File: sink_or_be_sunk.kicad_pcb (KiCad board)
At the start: 2 copper layers, 87 parts, among them J1 Keypad_Conn, J10 Grid_Conn, J11 Grid_Conn, J12 Grid_Conn, J13 Grid_Conn, J14 Grid_Conn, J15 Grid_Conn, J16 Grid_Conn, J17 Grid_Conn, J18 Grid_Conn, J19 Grid_Conn, J2 Mux_Conn, J20 Grid_Conn, J21 Grid_Conn, J22 Grid_Conn, J23 Grid_Conn, J3 Display_Conn, J4 JTAG_Conn, J5 Battery_Conn, J6 USB_B_Micro, J7 Debug_Conn, J8 Grid_Conn_LED, J9 Grid_Conn, M1 Motor_DC, Q1 IRL530, Q2 2N3704, Q3 2N3704, Q4 Q_PMOS_DGS, SW1 Reset_SW, SW2 SW_DPST, U1 SN74HC151N, U2 LDL1117-SMD, U3 MCP73831-2-OT, U4 MCP608, U5 ESP32-WROOM-32, U6 CY7C65213A-28PVXI

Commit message: before pin shift
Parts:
- moved J7 41.9 mm to (396.3, 130.0)
- moved TP2 14.8 mm to (476.7, 94.6)
- moved J4 14.6 mm to (490.9, 95.8)
- moved R24 14.0 mm to (485.4, 90.7)
- moved TP1 14.0 mm to (476.8, 100.2)
- moved R25 13.9 mm to (485.4, 93.3)
- moved R26 13.5 mm to (485.3, 95.8)
- moved R22 13.2 mm to (485.3, 88.2)
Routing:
- net /RXLED: track 0.00 -> 36.5 mm, vias 0 -> 1
- net /TXLED: track 0.00 -> 35.5 mm, vias 0 -> 1
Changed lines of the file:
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@@
     (thickness 1.6)
     (drawings 2)
-    (tracks 180)
+    (tracks 194)
     (zones 0)
     (modules 87)
@@
   )
   (module TestPoint:TestPoint_Plated_Hole_D2.0mm (layer F.Cu)
-    (at 464.058 86.868)
+    (at 476.7072 94.5896)
     (descr "Plated Hole as test Point, diameter 2.0mm")
     (tags "test point plated hole")
@@
   )
   (module TestPoint:TestPoint_Plated_Hole_D2.0mm (layer F.Cu)
-    (at 472.186 86.995)
+    (at 476.758 100.2284)
     (descr "Plated Hole as test Point, diameter 2.0mm")
     (tags "test point plated hole")
@@
   )
   (module Resistor_SMD:R_0805_2012Metric_Pad1.20x1.40mm_HandSolder (layer F.Cu)
-    (at 494.411 85.852)
+    (at 485.3084 95.8088)
     (descr "Resistor SMD 0805 (2012 Metric), square (rectangular) end terminal, IPC_7351 nominal with elongated pad for handsoldering. (Body size source: IPC-SM-782 page 72, https://www.pcb-3d.com/wordpress/wp-content/uploads/ipc-sm-782a_amendment_1_and_2.pdf), generated with kicad-footprint-generator")
     (tags "resistor handsolder")
@@
   )
   (module Resistor_SMD:R_0805_2012Metric_Pad1.20x1.40mm_HandSolder (layer F.Cu)
-    (at 494.157 82.423)
+    (at 485.394 93.2688)
     (descr "Resistor SMD 0805 (2012 Metric), square (rectangular) end terminal, IPC_7351 nominal with elongated pad for handsoldering. (Body size source: IPC-SM-782 page 72, https://www.pcb-3d.com/wordpress/wp-content/uploads/ipc-sm-782a_amendment_1_and_2.pdf), generated with kicad-footprint-generator")
     (tags "resistor handsolder")
@@
   )
   (module Resistor_SMD:R_0805_2012Metric_Pad1.20x1.40mm_HandSolder (layer F.Cu)
-    (at 494.157 79.756)
+    (at 485.394 90.7288)
     (descr "Resistor SMD 0805 (2012 Metric), square (rectangular) end terminal, IPC_7351 nominal with elongated pad for handsoldering. (Body size source: IPC-SM-782 page 72, https://www.pcb-3d.com/wordpress/wp-content/uploads/ipc-sm-782a_amendment_1_and_2.pdf), generated with kicad-footprint-generator")
     (tags "resistor handsolder")
@@
   )
   (module Resistor_SMD:R_0805_2012Metric_Pad1.20x1.40mm_HandSolder (layer F.Cu)
-    (at 493.141 77.597)
+    (at 485.3432 88.1888)
     (descr "Resistor SMD 0805 (2012 Metric), square (rectangular) end terminal, IPC_7351 nominal with elongated pad for handsoldering. (Body size source: IPC-SM-782 page 72, https://www.pcb-3d.com/wordpress/wp-content/uploads/ipc-sm-782a_amendment_1_and_2.pdf), generated with kicad-footprint-generator")
     (tags "resistor handsolder")
@@
   )
   (module Connector_PinHeader_2.54mm:PinHeader_1x02_P2.54mm_Vertical (layer F.Cu)
-    (at 436.245 142.621 270)
+    (at 396.2908 130.048 270)
     (descr "Through hole straight pin header, 1x02, 2.54mm pitch, single row")
     (tags "Through hole pin header THT 1x02 2.54mm single row")
@@
   )
   (module Connector_PinHeader_2.54mm:PinHeader_1x04_P2.54mm_Vertical (layer F.Cu)
-    (at 501.142 85.344 180)
+    (at 490.9312 95.8088 180)
     (descr "Through hole straight pin header, 1x04, 2.54mm pitch, single row")
     (tags "Through hole pin header THT 1x04 2.54mm single row")
@@
   (segment (start 448.183 97.0885) (end 448.269 97.1745) (width 0.254) (layer F.Cu) (net 2))
   (segment (start 448.183 95.005) (end 448.183 97.0885) (width 0.254) (layer F.Cu) (net 2))
-  (via (at 448.31 99.06) (size 0.762) (drill 0.381) (layers F.Cu B.Cu) (net 2))
-  (segment (start 448.269 99.019) (end 448.31 99.06) (width 0.254) (layer F.Cu) (net 2))
-  (segment (start 448.269 97.1745) (end 448.269 99.019) (width 0.254) (layer F.Cu) (net 2))
   (segment (start 449.453 111.134) (end 449.453 113.03) (width 0.8128) (layer F.Cu) (net 2))
   (segment (start 445.0625 106.7435) (end 449.453 111.134) (width 0.8128) (layer F.Cu) (net 2))
   (segment (start 445.019 103.346663) (end 444.551847 102.87951) (width 0.254) (layer F.Cu) (net 2))
-  (segment (start 448.31 99.06) (end 444.551847 102.818153) (width 0.254) (layer B.Cu) (net 2))
   (segment (start 445.019 104.3745) (end 445.019 103.346663) (width 0.254) (layer F.Cu) (net 2))
   (via (at 444.551847 102.87951) (size 0.762) (drill 0.381) (layers F.Cu B.Cu) (net 2))
+  (segment (start 448.269 97.1745) (end 448.269 99.019) (width 0.254) (layer F.Cu) (net 2))
   (segment (start 444.551847 102.818153) (end 444.551847 102.87951) (width 0.254) (layer B.Cu) (net 2))
+  (via (at 448.31 99.06) (size 0.762) (drill 0.381) (layers F.Cu B.Cu) (net 2))
+  (segment (start 448.31 99.06) (end 444.551847 102.818153) (width 0.254) (layer B.Cu) (net 2))
+  (segment (start 448.269 99.019) (end 448.31 99.06) (width 0.254) (layer F.Cu) (net 2))
   (segment (start 424.951 130.683) (end 425.069 130.565) (width 0.8128) (layer F.Cu) (net 3))
   (segment (start 421.8215 130.683) (end 424.951 130.683) (width 0.8128) (layer F.Cu) (net 3))
@@
   (segment (start 438.107 127.465) (end 440.055 129.413) (width 0.254) (layer F.Cu) (net 5))
   (segment (start 435.991 127.465) (end 438.107 127.465) (width 0.254) (layer F.Cu) (net 5))
+  (via (at 445.2112 99.9236) (size 0.762) (drill 0.381) (layers F.Cu B.Cu) (net 6))
+  (segment (start 445.3489 99.9236) (end 445.2112 99.9236) (width 0.254) (layer F.Cu) (net 6))
+  (segment (start 446.969 98.3035) (end 445.3489 99.9236) (width 0.254) (layer F.Cu) (net 6))
+  (segment (start 446.969 97.1745) (end 446.969 98.3035) (width 0.254) (layer F.Cu) (net 6))
+  (segment (start 474.881599 98.351999) (end 476.758 100.2284) (width 0.254) (layer B.Cu) (net 6))
+  (segment (start 447.970159 98.351999) (end 474.881599 98.351999) (width 0.254) (layer B.Cu) (net 6))
+  (segment (start 446.398558 99.9236) (end 447.970159 98.351999) (width 0.254) (layer B.Cu) (net 6))
+  (segment (start 445.2112 99.9236) (end 446.398558 99.9236) (width 0.254) (layer B.Cu) (net 6))
+  (via (at 445.3636 98.9076) (size 0.762) (drill 0.381) (layers F.Cu B.Cu) (net 7))
+  (segment (start 445.7149 98.9076) (end 445.3636 98.9076) (width 0.254) (layer F.Cu) (net 7))
+  (segment (start 446.319 98.3035) (end 445.7149 98.9076) (width 0.254) (layer F.Cu) (net 7))
+  (segment (start 446.319 97.1745) (end 446.319 98.3035) (width 0.254) (layer F.Cu) (net 7))
+  (segment (start 449.6816 94.5896) (end 476.7072 94.5896) (width 0.254) (layer B.Cu) (net 7))
+  (segment (start 445.3636 98.9076) (end 449.6816 94.5896) (width 0.254) (layer B.Cu) (net 7))
   (via (at 406.8445 116.205) (size 0.762) (drill 0.381) (layers F.Cu B.Cu) (net 24))
   (segment (start 406.0825 115.443) (end 406.8445 116.205) (width 0.254) (layer F.Cu) (net 24))

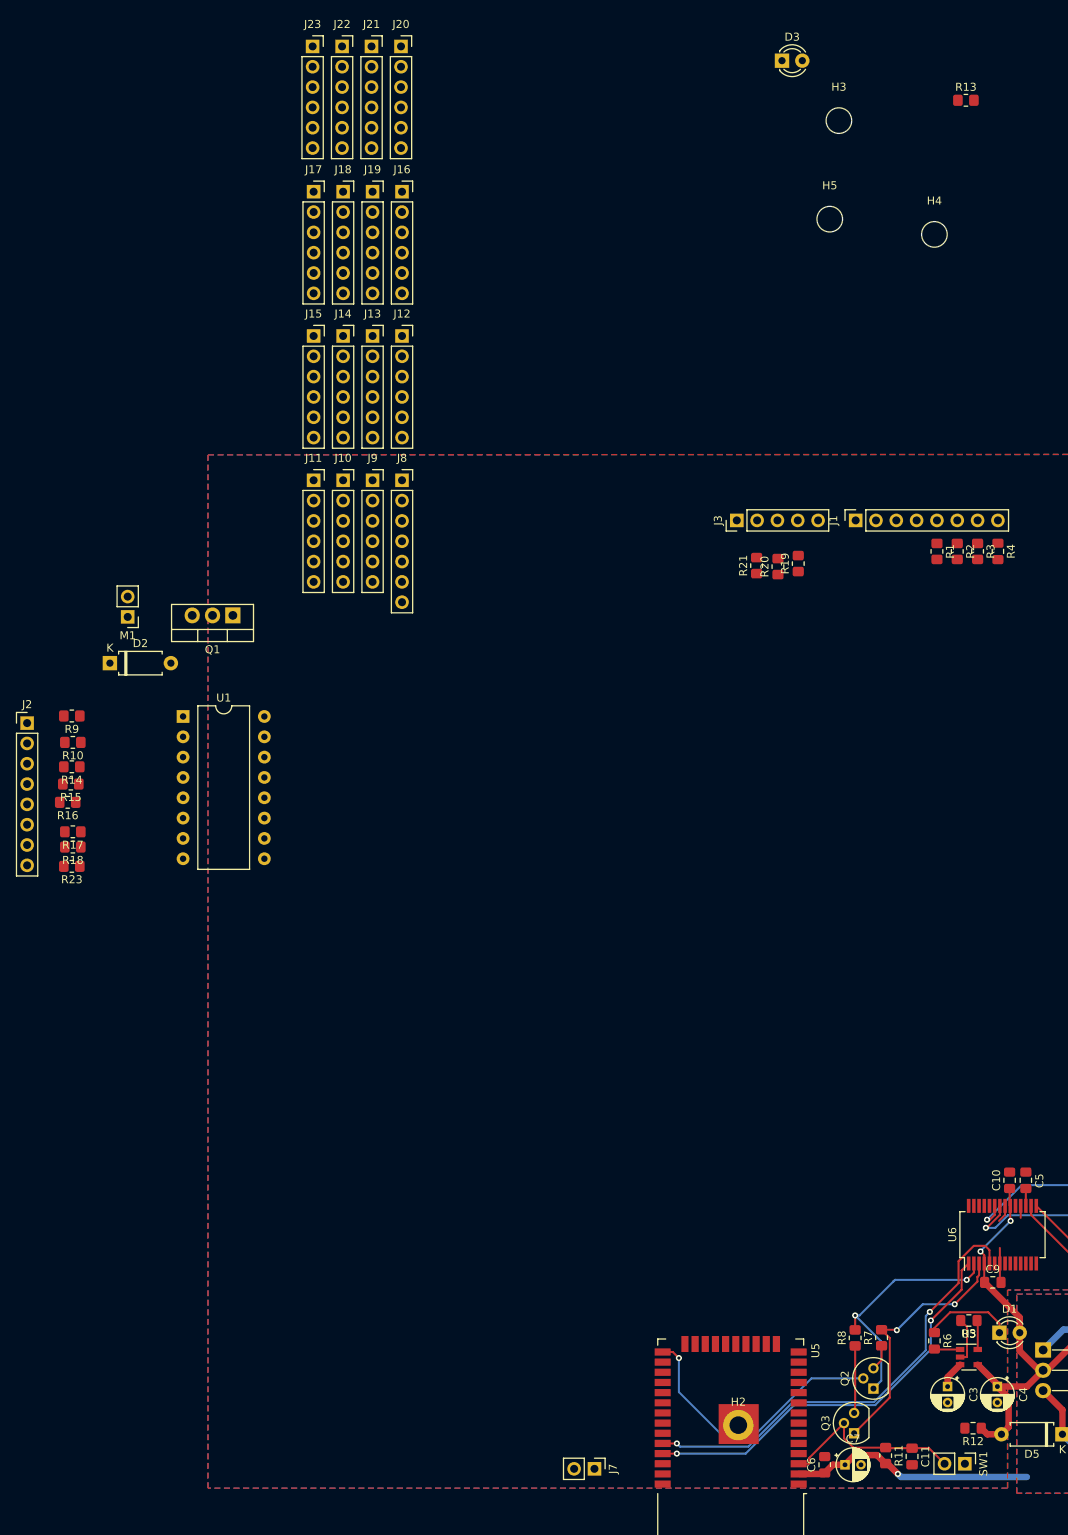
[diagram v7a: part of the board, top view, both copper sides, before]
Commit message: finsihed routing mux
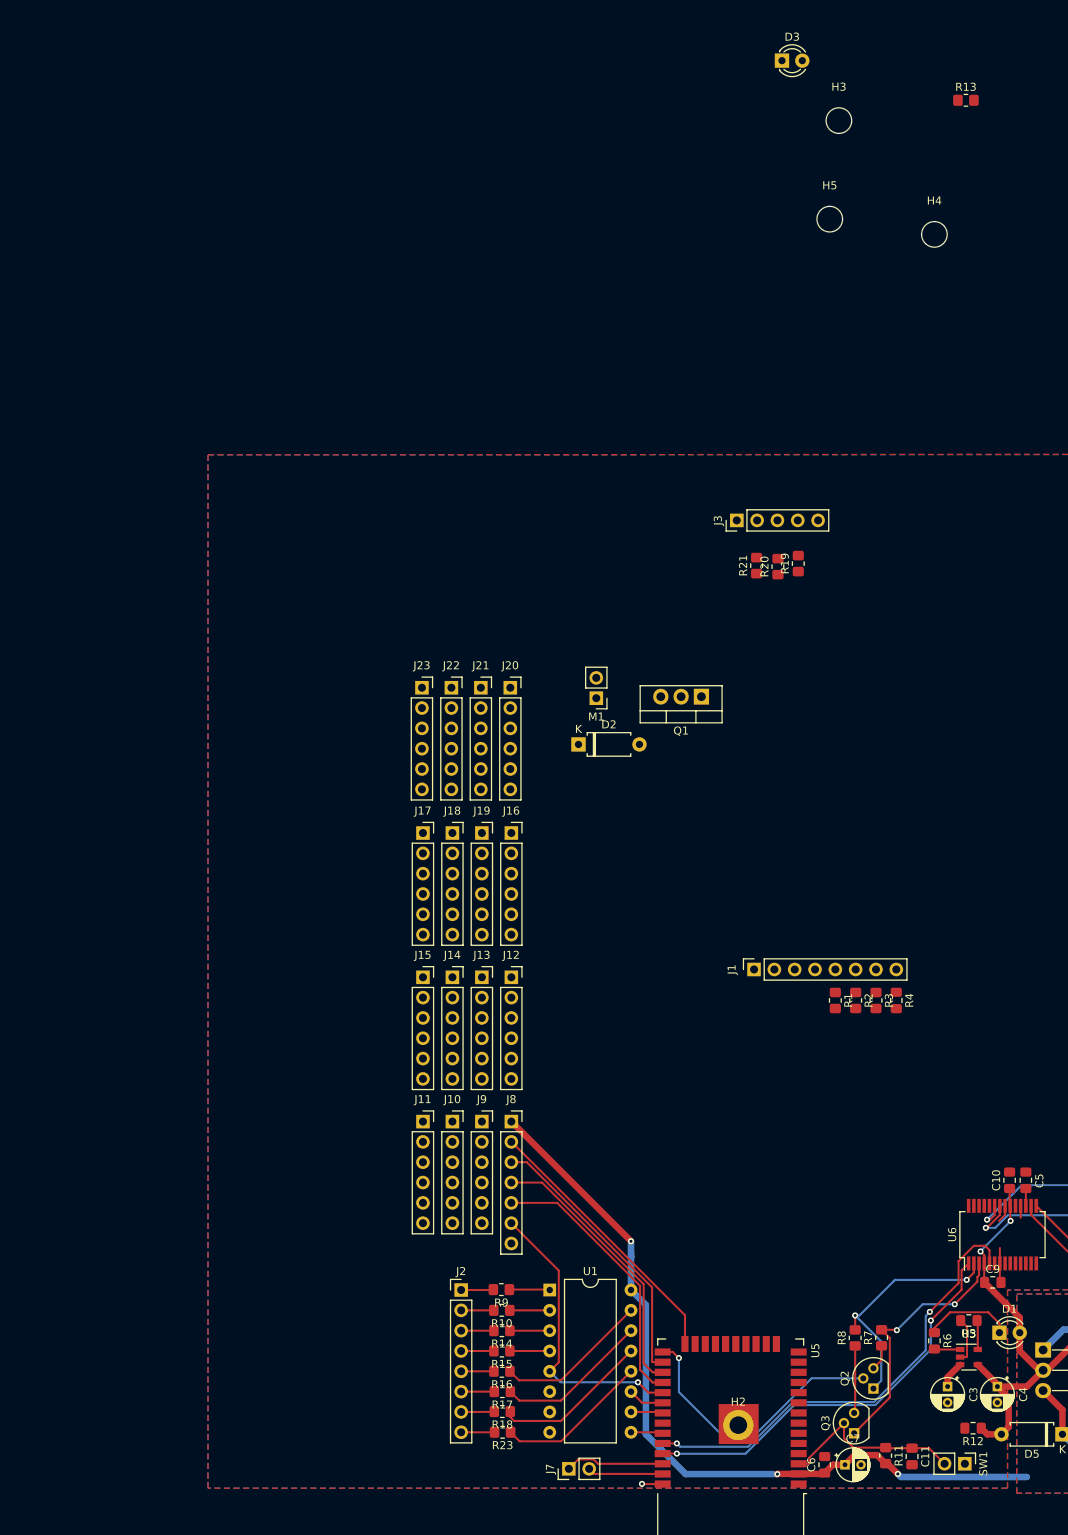
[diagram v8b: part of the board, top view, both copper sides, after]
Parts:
- moved R9 89.6 mm to (384.7, 107.6)
- moved R16 89.5 mm to (384.7, 117.9)
- moved J2 89.2 mm to (379.6, 107.7)
- moved R15 89.0 mm to (384.7, 115.3)
- moved R10 89.0 mm to (384.7, 110.2)
- moved R23 88.9 mm to (384.8, 125.5)
- moved R18 88.7 mm to (384.8, 122.9)
- moved R14 88.6 mm to (384.7, 112.8)
- moved R17 88.2 mm to (384.8, 120.4)
- moved U1 85.1 mm to (390.7, 107.7)
- moved J12 81.3 mm to (385.9, 68.6)
- moved J13 81.3 mm to (382.2, 68.6)
- moved J14 81.3 mm to (378.5, 68.6)
- moved J15 81.3 mm to (374.9, 68.6)
- moved J20 81.3 mm to (385.8, 32.4)
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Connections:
- J12 pad 2: /MUX_COL_SEL1 -> /LED_OUT
- J12 pad 3: /MUX_COL_SEL2 -> /MUX_COL_SEL1
- J12 pad 4: /MUX_COL_SEL0 -> /MUX_COL_SEL2
- J12 pad 5: /BOAT_INPUT -> /MUX_COL_SEL0
- J16 pad 2: /MUX_COL_SEL1 -> /LED_OUT
- J16 pad 3: /MUX_COL_SEL2 -> /MUX_COL_SEL1
- J16 pad 4: /MUX_COL_SEL0 -> /MUX_COL_SEL2
- J16 pad 5: /BOAT_INPUT -> /MUX_COL_SEL0
- J20 pad 2: /MUX_COL_SEL1 -> /LED_OUT
- J20 pad 3: /MUX_COL_SEL2 -> /MUX_COL_SEL1
- J20 pad 4: /MUX_COL_SEL0 -> /MUX_COL_SEL2
- J20 pad 5: /BOAT_INPUT -> /MUX_COL_SEL0
- J8 pad 2: /MUX_COL_SEL1 -> /LED_OUT
- J8 pad 3: /MUX_COL_SEL2 -> /MUX_COL_SEL1
- J8 pad 4: /MUX_COL_SEL0 -> /MUX_COL_SEL2
- J8 pad 5: /BOAT_INPUT -> /MUX_COL_SEL0
- J8 pad 6: /LED_OUT -> /BOAT_INPUT
- U5 pad 11: /KEYPAD_ROW1 -> /KEYPAD_COL3
- U5 pad 12: /KEYPAD_ROW0 -> /KEYPAD_COL2
- U5 pad 17: /KEYPAD_COL3 -> /KEYPAD_COL1
- U5 pad 18: /KEYPAD_COL2 -> /KEYPAD_COL0
- U5 pad 22: /KEYPAD_COL1 -> /MOTOR
- U5 pad 24: /KEYPAD_COL0 -> /LED_OUT
- U5 pad 26: /MOTOR -> /MUX_COL_SEL1
- U5 pad 27: /BOAT_INPUT -> /MUX_COL_SEL2
- U5 pad 28: /MUX_COL_SEL2 -> /MUX_COL_SEL0
- U5 pad 29: /MUX_COL_SEL1 -> /BOAT_INPUT
- U5 pad 30: /MUX_COL_SEL0 -> /MUX_ROW_SEL0
- U5 pad 31: /MUX_ROW_SEL0 -> /MUX_ROW_SEL1
- U5 pad 33: /MUX_ROW_SEL1 -> /MUX_ROW_SEL2
- U5 pad 36: /MUX_ROW_SEL2 -> /DBG1
- U5 pad 37: /LED_OUT -> /DBG2
- U5 pad 6: /DBG1 -> /KEYPAD_ROW3
- U5 pad 7: /DBG2 -> /KEYPAD_ROW2
- U5 pad 8: /KEYPAD_ROW3 -> /KEYPAD_ROW1
- U5 pad 9: /KEYPAD_ROW2 -> /KEYPAD_ROW0
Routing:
- net +3V3: track 30.6 -> 98.5 mm, vias 1 -> 3
- net /BOAT_INPUT: track 0.00 -> 36.7 mm, vias 0 -> 1
- net /MUX_COL_SEL1: track 0.00 -> 34.7 mm
- net /MUX_COL_SEL2: track 0.00 -> 34.5 mm
- net /MUX_COL_SEL0: track 0.00 -> 34.4 mm
- net /LED_OUT: track 0.00 -> 34.3 mm
- net /MUX_ROW6: track 0.00 -> 19.6 mm
- net /MUX_ROW4: track 0.00 -> 19.2 mm
- net /MUX_ROW5: track 0.00 -> 19.2 mm
- net /MUX_ROW7: track 0.00 -> 19.1 mm
- net /DBG1: track 0.00 -> 12.4 mm
- net /DBG2: track 0.00 -> 9.45 mm
- net /MUX_ROW3: track 0.00 -> 5.07 mm
- net /MUX_ROW2: track 0.00 -> 4.99 mm
- net /MUX_ROW1: track 0.00 -> 4.98 mm
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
